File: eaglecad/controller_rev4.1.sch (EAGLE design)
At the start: 79 parts, among them CON502 CARD CONN, U100 STM32L452XX_QFPN48, U101 TCAN330, U200 TPS63070, U300 STSPIN230, U301 TSV991ILT, U302 AS5047P, U400 STSPIN250, U401 TSV991ILT, X101 ABM10-16MHz

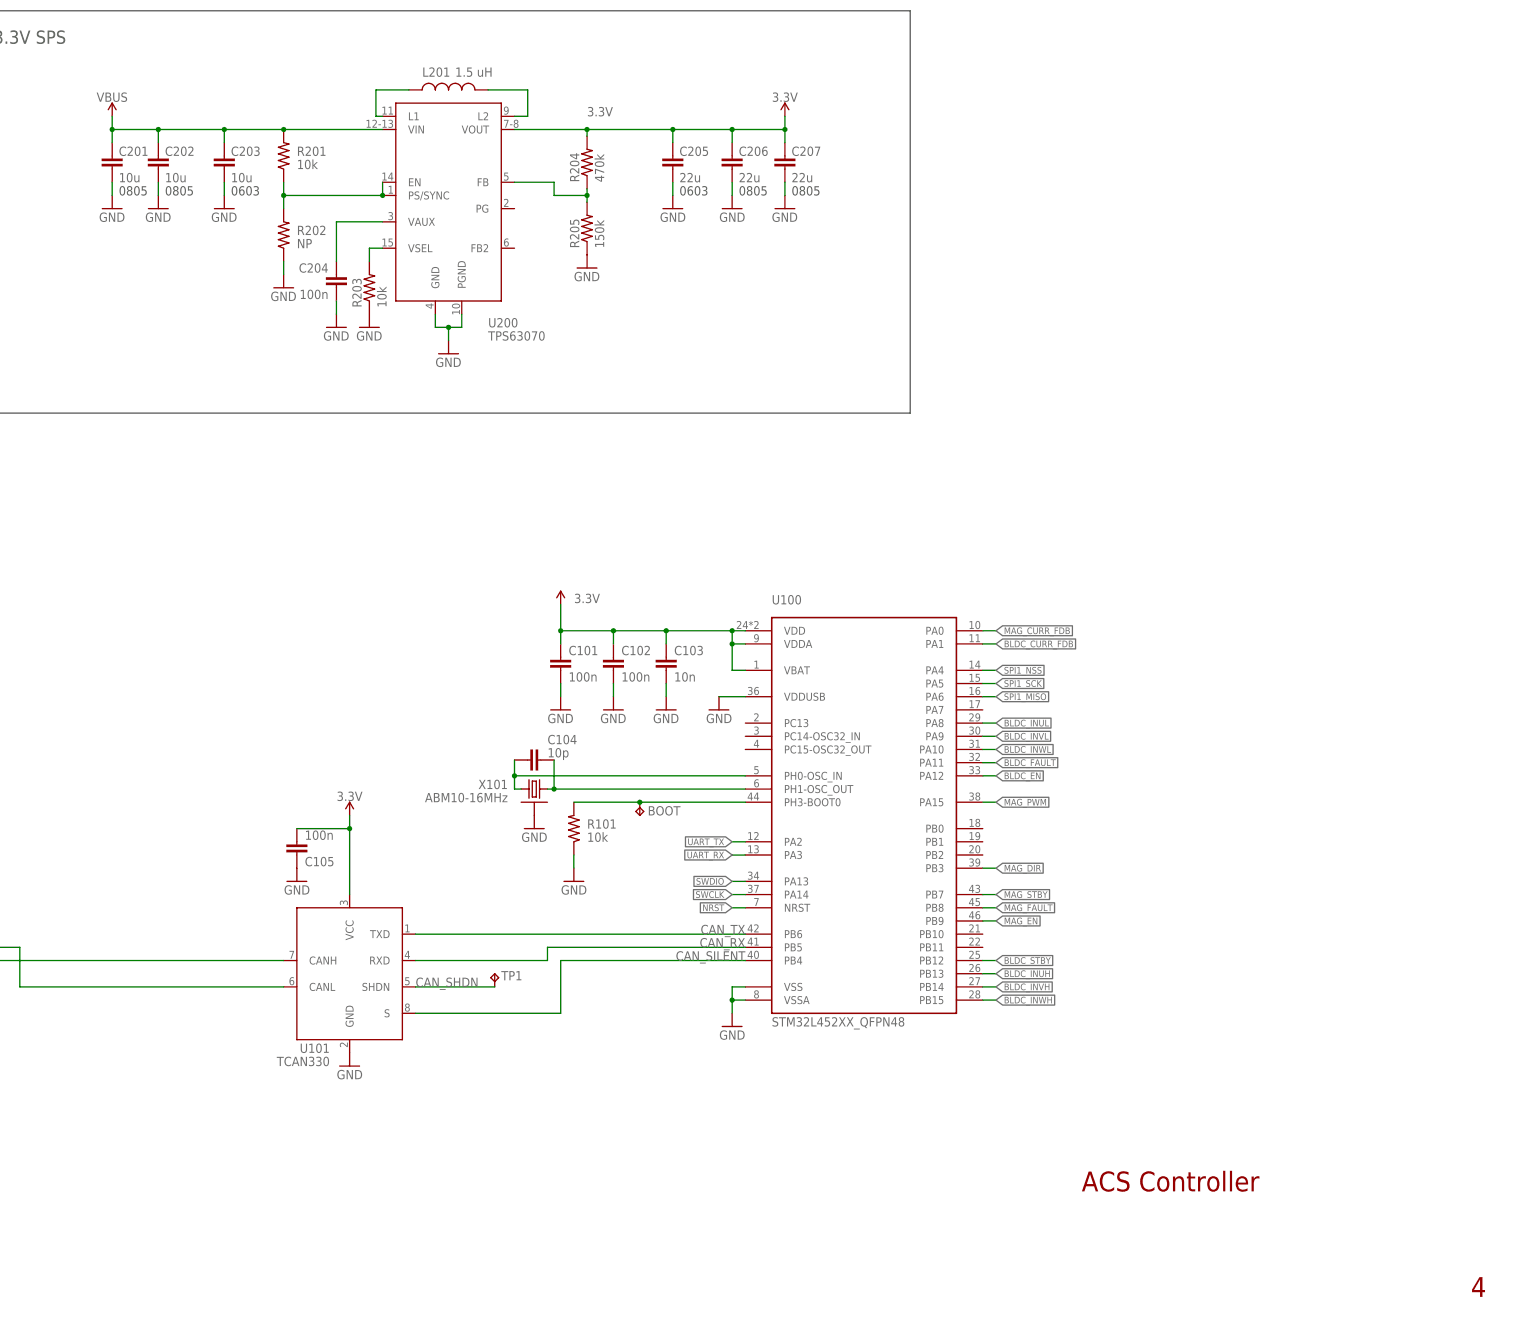
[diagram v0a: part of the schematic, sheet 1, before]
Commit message: Current set of modifications for Rev4.1 completed, some errors found and corrected
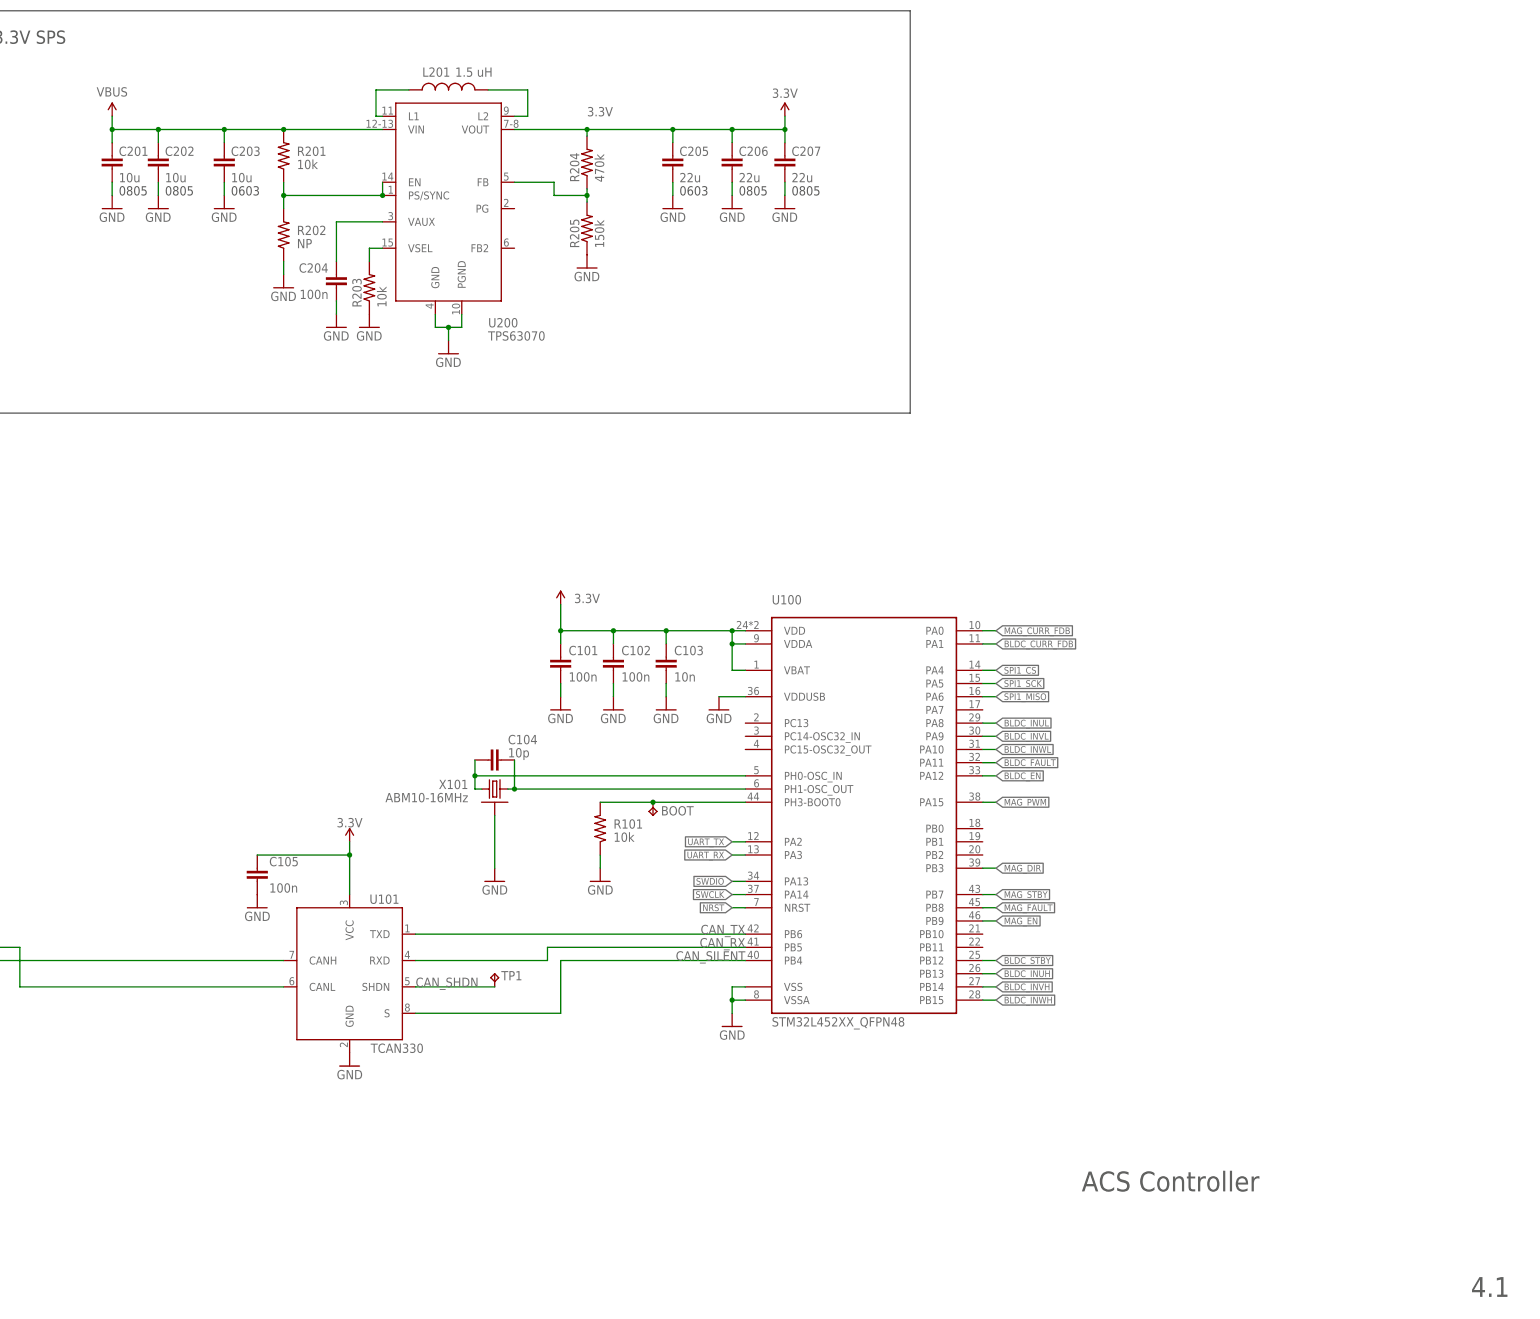
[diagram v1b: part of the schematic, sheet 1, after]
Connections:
- net SPI1_NSS renamed SPI1_CS
- removed net V_BATT: C501.1
- net 3.3V: now also C105.1; no longer C105.2
- net GND: now also C105.2; no longer C105.1
- net VBUS: now also C501.1
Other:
- note added: "4.1"
- note removed: "4"
- moved on the sheet: BOOT, C104, C105, R101, X101
